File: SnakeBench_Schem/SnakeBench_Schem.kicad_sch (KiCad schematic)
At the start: 12 parts, among them J1 ATX-24, SW1 SW_DIP_x01, U1 WZ3605E_Adjust-Voltage

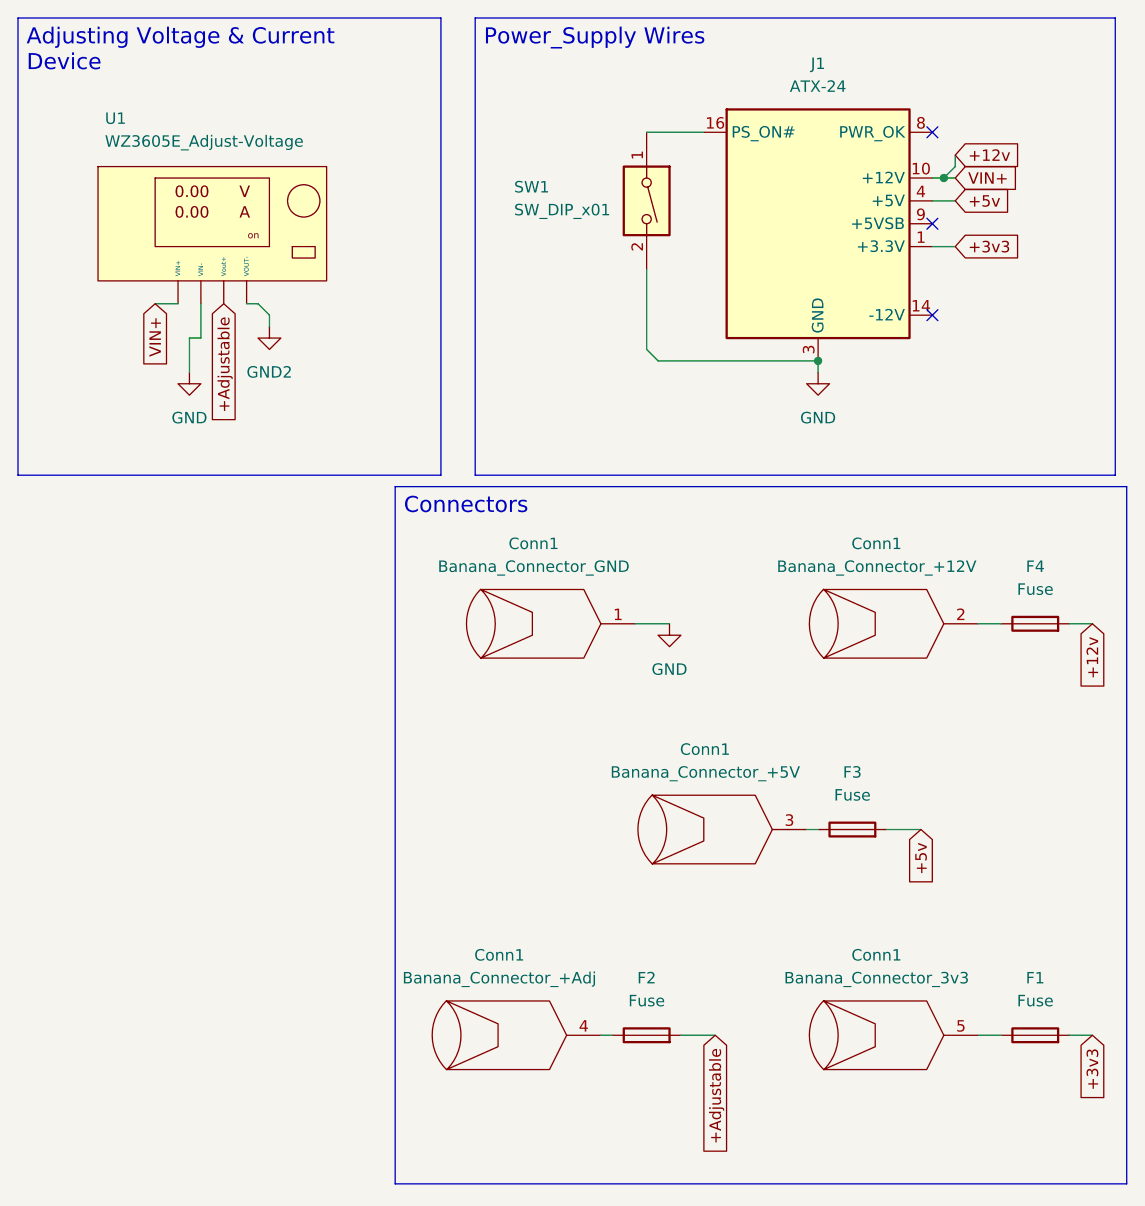
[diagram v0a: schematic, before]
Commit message: Fixed Bananas footprint problem
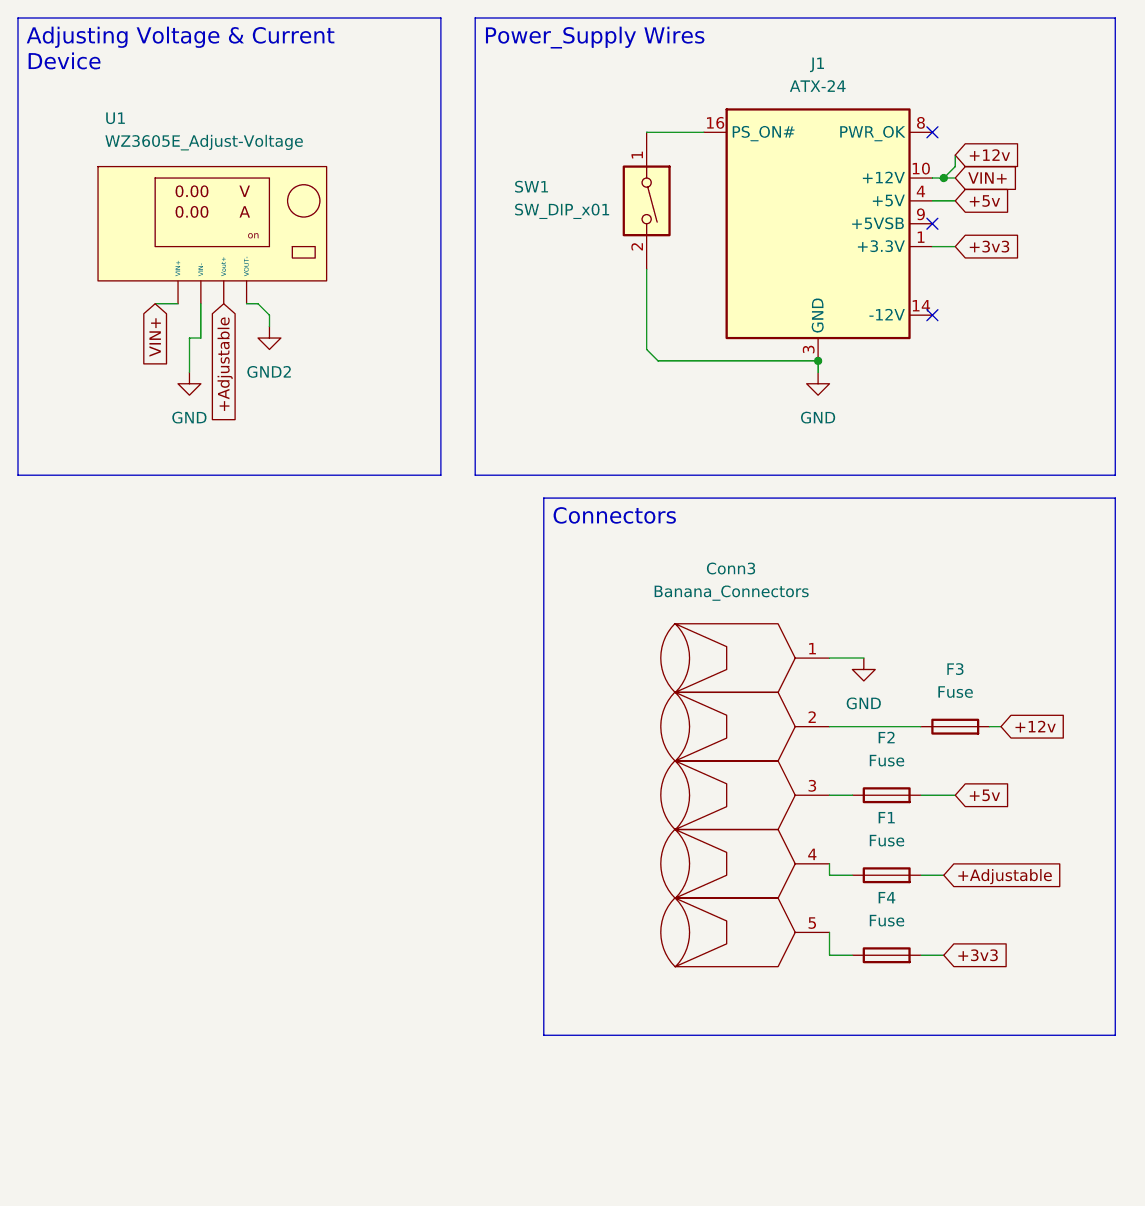
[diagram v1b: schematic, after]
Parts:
- removed Conn1: Banana_Connector_+Adj, TerminalBlock_Altech:Altech_AK100_1x02_P5.00mm, symbol RAM-Components:Banana_Connector
- removed Conn1: Banana_Connector_GND, TerminalBlock_Altech:Altech_AK100_1x02_P5.00mm, symbol RAM-Components:Banana_Connector
- removed Conn1: Banana_Connector_+12V, TerminalBlock_Altech:Altech_AK100_1x02_P5.00mm, symbol RAM-Components:Banana_Connector
- removed Conn1: Banana_Connector_3v3, TerminalBlock_Altech:Altech_AK100_1x02_P5.00mm, symbol RAM-Components:Banana_Connector
- Conn3: renamed from Conn1; value Banana_Connector_+5V -> Banana_Connectors; footprint TerminalBlock_Altech:Altech_AK100_1x02_P5.00mm -> TerminalBlock_Altech:Altech_AK100_1x05_P5.00mm
- J1: footprint Connector_PinHeader_1.00mm:PinHeader_2x12_P1.00mm_Vertical -> Connector_PinHeader_2.54mm:PinHeader_2x12_P2.54mm_Vertical
- renumbered F2 to F1, F3 to F2, F4 to F3, F1 to F4
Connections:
- net GND: now also Conn3.1 (Pin_1)
- net at F4.1: now also Conn3.5 (Pin_1)
- net at F3.1: now also Conn3.2 (Pin_1)
- net at F1.1: now also Conn3.4 (Pin_1)
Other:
- moved on the sheet: F1, F2, F3, F4

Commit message: Update & fix the impossible width problem
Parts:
- removed J1: ATX-24, Connector_PinHeader_2.54mm:PinHeader_2x12_P2.54mm_Vertical, symbol Connector:ATX-24
- added J1: From_Supply, symbol Connector:Conn_01x05_Pin
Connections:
- net +12v: now also U1.1 (VIN+), J1.3 (Pin_3); no longer U1. (VOUT-)
- net +3v3: now also J1.5 (Pin_5)
- net +5v: now also J1.4 (Pin_4)
- net +Adjustable: now also U1.3 (Vout+); no longer U1. (VOUT-)
- net GND: now also U1.2 (VIN-), J1.1 (Pin_1); no longer U1. (VOUT-)
- net GND2: now also U1.4 (VOUT-); no longer U1. (VOUT-)
- net at SW1.1: now also J1.2 (Pin_2)
- no-connect marks 3 -> 0

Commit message: Finished the PCB, fixed something in the Schem
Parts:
- Conn3: footprint TerminalBlock_Altech:Altech_AK100_1x05_P5.00mm -> TerminalBlock_Altech:Altech_AK100_1x06_P5.00mm
- J1: footprint (none) -> TerminalBlock_Altech:Altech_AK100_1x05_P5.00mm
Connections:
- net +12v: now also F4.2, J1.4 (Pin_4); no longer F3.2, J1.3 (Pin_3)
- net +3v3: now also F3.2; no longer F4.2
- net +5v: now also F1.2, J1.3 (Pin_3); no longer F2.2, J1.4 (Pin_4)
- net +Adjustable: now also F2.2; no longer F1.2
- net GND2: now also Conn3.6 (Pin_1)
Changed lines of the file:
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@@
 		(exclude_from_sim no)
 		(at 218.44 72.39 0)
-		(size 63.5 59.69)
+		(size 63.5 64.77)
 		(margins 0.9525 0.9525 0.9525 0.9525)
 		(stroke
@@
 	)
 	(junction
-		(at 247.65 36.83)
+		(at 250.19 36.83)
 		(diameter 0)
 		(color 0 0 0 0)
@@
 	(wire
 		(pts
-			(xy 247.65 36.83) (xy 247.65 38.1)
+			(xy 247.65 26.67) (xy 247.65 38.1)
 		)
 		(stroke
@@
 	(wire
 		(pts
-			(xy 250.19 35.56) (xy 250.19 38.1)
+			(xy 255.27 128.27) (xy 250.19 128.27)
+		)
+		(stroke
+			(width 0)
+			(type default)
+		)
+	)
+	(wire
+		(pts
+			(xy 250.19 35.56) (xy 250.19 36.83)
 		)
 		(stroke
@@
 	(wire
 		(pts
+			(xy 250.19 36.83) (xy 250.19 38.1)
+		)
+		(stroke
+			(width 0)
+			(type default)
+		)
+	)
+	(wire
+		(pts
 			(xy 236.22 41.91) (xy 236.22 43.18)
 		)
@@
 	(wire
 		(pts
-			(xy 246.38 35.56) (xy 247.65 36.83)
-		)
-		(stroke
-			(width 0)
-			(type default)
-		)
-	)
-	(wire
-		(pts
 			(xy 179.07 58.42) (xy 179.07 54.61)
 		)
@@
 	(wire
 		(pts
+			(xy 246.38 36.83) (xy 250.19 36.83)
+		)
+		(stroke
+			(width 0)
+			(type default)
+		)
+	)
+	(wire
+		(pts
 			(xy 186.69 50.8) (xy 187.96 52.07)
 		)
@@
 	(wire
 		(pts
-			(xy 247.65 35.56) (xy 247.65 36.83)
-		)
-		(stroke
-			(width 0)
-			(type default)
-		)
-	)
-	(wire
-		(pts
 			(xy 240.03 38.1) (xy 236.22 41.91)
 		)
@@
 	(wire
 		(pts
-			(xy 245.11 35.56) (xy 246.38 35.56)
+			(xy 243.84 33.02) (xy 246.38 33.02)
+		)
+		(stroke
+			(width 0)
+			(type default)
+		)
+	)
+	(wire
+		(pts
+			(xy 246.38 33.02) (xy 246.38 36.83)
 		)
 		(stroke
@@
 	(global_label "+5v"
 		(shape input)
-		(at 250.19 35.56 90)
+		(at 247.65 26.67 90)
 		(fields_autoplaced yes)
 		(effects
@@
 		)
 		(property "Intersheetrefs" "${INTERSHEET_REFS}"
-			(at 250.19 28.8253 90)
+			(at 247.65 19.0885 90)
 			(hide yes)
 			(show_name no)
@@
 	(global_label "+12v"
 		(shape input)
-		(at 269.24 97.79 0)
+		(at 262.89 123.19 0)
 		(fields_autoplaced yes)
 		(effects
@@
 		)
 		(property "Intersheetrefs" "${INTERSHEET_REFS}"
-			(at 277.1842 97.79 0)
+			(at 270.8342 123.19 0)
 			(hide yes)
 			(show_name no)
@@
 	(global_label "+3v3"
 		(shape input)
-		(at 262.89 123.19 0)
+		(at 269.24 97.79 0)
 		(fields_autoplaced yes)
 		(effects
@@
 		)
 		(property "Intersheetrefs" "${INTERSHEET_REFS}"
-			(at 270.8342 123.19 0)
+			(at 277.1842 97.79 0)
 			(hide yes)
 			(show_name no)
@@
 	(global_label "VIN+"
 		(shape input)
-		(at 247.65 35.56 90)
+		(at 250.19 35.56 90)
 		(fields_autoplaced yes)
 		(effects
@@
 		)
 		(property "Intersheetrefs" "${INTERSHEET_REFS}"
-			(at 247.65 27.9785 90)
+			(at 250.19 28.8253 90)
 			(hide yes)
 			(show_name no)
@@
 	(global_label "+Adjustable"
 		(shape input)
-		(at 262.89 114.3 0)
+		(at 264.16 105.41 0)
 		(fields_autoplaced yes)
 		(effects
@@
 		)
 		(property "Intersheetrefs" "${INTERSHEET_REFS}"
-			(at 277.2446 114.3 0)
+			(at 270.8947 105.41 0)
 			(hide yes)
 			(show_name no)
@@
 	(global_label "+5v"
 		(shape input)
-		(at 264.16 105.41 0)
+		(at 262.89 114.3 0)
 		(fields_autoplaced yes)
 		(effects
@@
 		)
 		(property "Intersheetrefs" "${INTERSHEET_REFS}"
-			(at 270.8947 105.41 0)
+			(at 277.2446 114.3 0)
 			(hide yes)
 			(show_name no)
@@
 	(global_label "+12v"
 		(shape input)
-		(at 245.11 35.56 90)
+		(at 243.84 33.02 90)
 		(fields_autoplaced yes)
 		(effects
@@
 		)
 		(property "Intersheetrefs" "${INTERSHEET_REFS}"
-			(at 245.11 27.6158 90)
+			(at 243.84 25.0758 90)
 			(hide yes)
 			(show_name no)
@@
 			)
 		)
-		(property "Footprint" ""
+		(property "Footprint" "TerminalBlock_Altech:Altech_AK100_1x05_P5.00mm"
 			(at 247.65 43.18 0)
 			(hide yes)
@@
 			)
 		)
-		(property "Footprint" "TerminalBlock_Altech:Altech_AK100_1x05_P5.00mm"
+		(property "Footprint" "TerminalBlock_Altech:Altech_AK100_1x06_P5.00mm"
 			(at 239.776 85.598 0)
 			(hide yes)
@@
 		)
 		(pin "4"
+		)
+		(pin "6"
 		)
 		(instances
@@
 					(unit 1)
 				)
+			)
+		)
+	)
+	(symbol
+		(lib_id "power:GND2")
+		(at 255.27 128.27 0)
+		(unit 1)
+		(body_style 1)
+		(exclude_from_sim no)
+		(in_bom yes)
+		(on_board yes)
+		(in_pos_files yes)
+		(dnp no)
+		(fields_autoplaced yes)
+		(property "Reference" "#PWR05"
+			(at 255.27 134.62 0)
+			(hide yes)
+			(show_name no)
+			(do_not_autoplace no)
+			(effects
+				(font
+					(size 1.27 1.27)
+				)
+			)
+		)
+		(property "Value" "GND2"
+			(at 255.27 133.35 0)
+			(show_name no)
+			(do_not_autoplace no)
+			(effects
+				(font
+					(size 1.27 1.27)
+				)
+			)
+		)
+		(property "Footprint" ""
+			(at 255.27 128.27 0)
+			(hide yes)
+			(show_name no)
+			(do_not_autoplace no)
+			(effects
+				(font
+					(size 1.27 1.27)
+				)
+			)
+		)
+		(property "Datasheet" ""
+			(at 255.27 128.27 0)
+			(hide yes)
+			(show_name no)
+			(do_not_autoplace no)
+			(effects
+				(font
+					(size 1.27 1.27)
+				)
+			)
+		)
+		(property "Description" "Power symbol creates a global label with name \"GND2\" , ground"
+			(at 255.27 128.27 0)
+			(hide yes)
+			(show_name no)
+			(do_not_autoplace no)
+			(effects
+				(font
+					(size 1.27 1.27)
+				)
+			)
+		)
+		(pin "1"
+		)
+		(instances
+			(project "SnakeBench_Schem"
+				(path "/996e77d2-53ba-40ea-9cac-ec9750258f54"
+					(reference "#PWR05")
+					(unit 1)
+				)
